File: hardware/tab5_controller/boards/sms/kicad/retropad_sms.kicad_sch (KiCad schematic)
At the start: 46 parts, among them J1 Tab5 Ext.Port1, J2 SWD, SW1 UP, SW10 START, SW11 MENU, SW12 L, SW13 R, SW2 DOWN, SW3 LEFT, SW4 RIGHT, SW5 X, SW6 B, SW7 Y, SW8 A, SW9 SELECT, U1 STM32F030C8T6

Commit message: tab5_controller: NES, Game Boy, Genesis and SMS/GG boards; shared generators
Generators move from boards/snes/kicad to boards/kicad_gen and take a
console name (gen_pcb.py, gen_sch.py, check_netlist.py, plus render.py);
console ids, titles and ID straps come from layout.CONSOLES.

New layouts in layout.py, each passing the clearance checks:
- NES (ID 1): B/A side by side, flat SELECT/START, MENU
- Game Boy (ID 2): diagonal B/A, flat SELECT/START (the angled pair left
  ROW7 unroutable), MENU
- Genesis (ID 5): A/B/C rising row, START, MENU
- Master System / Game Gear (ID 4): 1/2 on the B/A bits, START, MENU

All five boards are regenerated: routed with 0 unconnected pads and no
clearance/edge errors, schematic vs PCB 0 differences, ID straps and
button matrix wiring verified. Connector GND pins and SMD pads now join
the GND pour solidly, which removes starved-thermal errors.

Co-Authored-By: Claude Opus 5.5 <noreply@anthropic.com>
Claude-Session: https://claude.ai/code/session_01NhSHTsezreiVZCnuBhQzP2
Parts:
- removed D10, D11, D12, D13, D9: 1N4148W, Diode_SMD:D_SOD-123, symbol Device:D
- removed SW10: START, Button_Switch_THT:SW_PUSH_6mm, symbol Switch:SW_Push
- removed SW11: MENU, Button_Switch_THT:SW_PUSH_6mm, symbol Switch:SW_Push
- removed SW12: L, Button_Switch_THT:SW_Tactile_SPST_Angled_PTS645Vx31-2LFS, symbol Switch:SW_Push
- removed SW13: R, Button_Switch_THT:SW_Tactile_SPST_Angled_PTS645Vx31-2LFS, symbol Switch:SW_Push
- removed SW9: SELECT, Button_Switch_THT:SW_PUSH_6mm, symbol Switch:SW_Push
- R6, R7: value 0R -> DNP; now not fitted; now left out of the parts list
- R8: value DNP -> 0R; now fitted; now in the parts list
- SW5: value X -> 1
- SW6: value B -> 2
- SW7: value Y -> START; footprint Button_Switch_THT:SW_PUSH-12mm -> Button_Switch_THT:SW_PUSH_6mm
- SW8: value A -> MENU; footprint Button_Switch_THT:SW_PUSH-12mm -> Button_Switch_THT:SW_PUSH_6mm
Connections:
- net K_A is gone; now on net K_MENU: D8.1 (K), SW8.1
- net K_Y is gone; now on net K_START: D7.1 (K), SW7.1
- net COL0: no longer SW8.2
- net COL2: now also SW8.2
- net ROW0: now also D8.2 (A); no longer D7.2 (A)
- net ROW4: now also D6.2 (A); no longer D8.2 (A)
- net ROW5: now also D5.2 (A); no longer D6.2 (A)
- net ROW6: now also D7.2 (A)
- net ROW7: no longer D5.2 (A)
- net K_B renamed K_2
- net K_X renamed K_1
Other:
- note added: "1"
- note added: "2"
- note added: "Console ID straps: 0R to GND = bit set. Master System / Game Gear = ID 4 (fit R8; R6, R7, R9, R10 DNP)"
- note removed: "A"
- note removed: "B"
- note removed: "Console ID straps: 0R to GND = bit set. SNES = ID 3 (fit R6, R7; R8, R9, R10 DNP)"
- note removed: "L"
- note removed: "R"
- note removed: "SELECT"
- note removed: "X"
- note removed: "Y"
- title: RetroPad SNES controller (console ID 3) -> RetroPad Master System / Game Gear controller (console ID 4)

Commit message: tab5_controller: build every console board on the AVR32DD28
The STM32F030 matrix boards are gone. SNES, NES, Game Boy, Genesis and
Master System / Game Gear are now all AVR32DD28 boards: one MCU pin per
button, no diodes, UPDI programming, one firmware image (firmware_avrdd)
keyed by the console-ID straps.

- layout.py / gen_pcb.py / gen_sch.py: drop the stm32 core (LQFP-48,
  key matrix, diodes, SWD header, AN_EN strap); the AVR DD core is the
  only one, and the *_dd board names become the plain console names.
- SNES, NES and Genesis keep the routing of their AVR DD prototypes;
  Game Boy and Master System are routed fresh.
- Every board: DRC 0 unconnected (silkscreen warnings only), schematic
  vs PCB 0 differences, and each switch checked against the MCU pin
  pinmap.h gives it for that console ID.
- Host test now also covers the Game Boy and Master System pin maps.
- READMEs describe the AVR DD boards only.

Co-Authored-By: Claude Opus 5.5 <noreply@anthropic.com>
Claude-Session: https://claude.ai/code/session_01NhSHTsezreiVZCnuBhQzP2
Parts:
- removed C5: 100nF, Capacitor_SMD:C_0603_1608Metric, symbol Device:C
- removed D1, D2, D3, D4, D5, D6, D7, D8: 1N4148W, Diode_SMD:D_SOD-123, symbol Device:D
- removed R10: DNP, Resistor_SMD:R_0603_1608Metric, symbol Device:R
- removed R4, R5: 10k, Resistor_SMD:R_0603_1608Metric, symbol Device:R
- added R11: DNP, Resistor_SMD:R_0603_1608Metric, symbol Device:R
- J2: value SWD -> UPDI; footprint Connector_PinHeader_2.54mm:PinHeader_1x05_P2.54mm_Vertical -> Connector_PinHeader_2.54mm:PinHeader_1x03_P2.54mm_Vertical; symbol Connector_Generic:Conn_01x05 -> Connector_Generic:Conn_01x03
- U1: value STM32F030C8T6 -> AVR32DD28-I/SO; footprint Package_QFP:LQFP-48_7x7mm_P0.5mm -> Package_SO:SOIC-28W_7.5x17.9mm_P1.27mm; symbol MCU_ST_STM32F0:STM32F030C8Tx -> RetroPad:AVR32DD28-xSO
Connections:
- net COL3 is gone; now on net K_START: U1.13 (PD7)
- net ROW2 is gone; now on net +3V3: U1.20 (VDD)
- net +3V3: now also U1.14 (VDD), U1.6 (VDDIO2); no longer U1.1 (VDD), U1.24 (VDD), U1.48 (VDD), U1.9 (VDDA)
- net GND: now also J2.3 (Pin_3), SW1.2, SW2.2, SW3.2, SW4.2, SW5.2, SW6.2, SW7.2, SW8.2, U1.15 (GND), U1.21 (GND); no longer J2.5 (Pin_5), U1.23 (VSS), U1.47 (VSS), U1.8 (VSSA)
- net ID0: now also U1.22 (XTALHF1/PA0); no longer U1.25 (PB12)
- net ID1: now also U1.23 (XTALHF2/PA1); no longer U1.26 (PB13)
- net ID2: now also U1.28 (PA6); no longer U1.27 (PB14)
- net ID3: now also U1.1 (PA7); no longer U1.45 (PB8)
- net K_1: now also U1.11 (PD5)
- net K_2: now also U1.12 (PD6)
- net K_DOWN: now also U1.8 (PD2)
- net K_LEFT: now also U1.9 (PD3)
- net K_MENU: now also U1.2 (PC0)
- net K_RIGHT: now also U1.10 (PD4)
- net K_UP: now also U1.7 (PD1)
- net SCL: now also U1.25 (PA3); no longer U1.21 (PB10)
- net SDA: now also U1.24 (PA2); no longer U1.22 (PB11)
- net G9_UPDI: now reaches J1.10 (Pin_10)
- net G9_UPDI: now also R11.2
- removed net AN_EN: U1.46 (PB9)
- removed net BOOT0: U1.44 (BOOT0)
- removed net COL0: SW1.2, SW2.2, SW3.2, SW4.2, SW5.2, SW6.2, U1.10 (PA0)
- removed net COL1: SW7.2, U1.11 (PA1)
- removed net COL2: SW8.2, U1.12 (PA2)
- removed net INT: J1.9 (Pin_9), R3.2, U1.38 (PA15)
- removed net NRST: J2.4 (Pin_4), U1.7 (NRST)
- net ROW0 renamed RESET
- net RESET: now also R3.2
- net ROW1 renamed UPDI
- net UPDI: now also J2.2 (Pin_2), R11.1
- removed net ROW3: U1.39 (PB3)
- removed net ROW4: U1.40 (PB4)
- removed net ROW5: U1.41 (PB5)
- removed net ROW6: U1.42 (PB6)
- removed net ROW7: U1.43 (PB7)
- removed net SWCLK: J2.2 (Pin_2), U1.37 (PA14)
- removed net SWDIO: J2.3 (Pin_3), U1.34 (PA13)
- new net AN0: U1.26 (PA4)
- new net AN1: U1.27 (PA5)
- no-connect marks 20 -> 8
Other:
- note added: "Buttons — one MCU pin each, switch to GND (internal pull-up); slot table in firmware_avrdd/pinmap.h"
- note added: "Console ID straps: 0R to GND = bit set. Master System / Game Gear = ID 4 (fit R8; R6, R7, R9 DNP)"
- note added: "Decoupling (VDD x2, VDDIO2), I2C pull-ups, RESET pull-up"
- note added: "MCU — AVR32DD28 (SOIC-28) running firmware_avrdd (I2C client 0x6D, RetroPad protocol)"
- note added: "PD1-PD7, PC0-PC3, PF0-PF1: one button per pin (internal pull-ups)"
- note added: "R11 (DNP): UPDI to J1 pin 10 / G9 — experimental in-system programming from the Tab5"
- note added: "UPDI programming (SerialUPDI / MPLAB Snap)"
- note removed: "Button matrix — row driven high, column read with pull-down; diode anode on the row"
- note removed: "Console ID straps: 0R to GND = bit set. Master System / Game Gear = ID 4 (fit R8; R6, R7, R9, R10 DNP)"
- note removed: "Decoupling, pull-ups, reset, BOOT0 (copied from the M5Stack keyboard)"
- note removed: "MCU — STM32F030C8T6 running the RetroPad firmware (I2C slave 0x6D)"
- note removed: "SWD (same order as the keyboard's P2)"
- moved on the sheet: C4, SW1, SW2, SW3, SW4, SW5, SW6, SW7, SW8

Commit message: tab5_controller: remove the UPDI-to-G9 link (R11) from every board
The Tab5 never updates controller firmware, so J1 pin 10 (G9) is left
unconnected, as on M5Stack's keyboard, and R11 and the G9_UPDI net are
gone. Boards are programmed only through their own UPDI header J2.

All five boards are re-routed (the old routes ended at R11). Game Boy
is routed with Freerouting 2.1 single-threaded because 1.9 stalls with
UPDI unrouted on it. Every board: DRC 0 unconnected pads (silkscreen
warnings only), schematic vs PCB 0 differences, switches on the pins
pinmap.h expects.

Co-Authored-By: Claude Opus 5.5 <noreply@anthropic.com>
Claude-Session: https://claude.ai/code/session_01NhSHTsezreiVZCnuBhQzP2
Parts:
- removed R11: DNP, Resistor_SMD:R_0603_1608Metric, symbol Device:R
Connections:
- net G9_UPDI: no longer names the net of J1.10 (Pin_10)
- no-connect marks 8 -> 9
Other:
- note removed: "R11 (DNP): UPDI to J1 pin 10 / G9 — experimental in-system programming from the Tab5"
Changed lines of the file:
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@@
       (project "retropad_sms" (path "/a309cff3-1dfb-5baa-b184-d84380f3c827" (reference "J1") (unit 1)))))
   (no_connect (at 170.18 39.37))
-  (wire
-    (pts (xy 182.88 49.53) (xy 190.5 49.53))
-    (stroke (width 0) (type default))
-)
-  (global_label
-    "G9_UPDI"
-    (shape bidirectional)
-    (at 190.5 49.53 0)
-    (fields_autoplaced)
-    (effects (font (size 1.27 1.27)) (justify left))
-    (property
-      "Intersheetrefs"
-      "${INTERSHEET_REFS}"
-      (at 190.5 49.53 0)
-      (effects (font (size 1.27 1.27)) hide)))
+  (no_connect (at 182.88 49.53))
   (wire
     (pts (xy 182.88 39.37) (xy 190.5 39.37))
@@
         (path "/a309cff3-1dfb-5baa-b184-d84380f3c827" (reference "#PWR17") (unit 1)))))
   (text
-    "R11 (DNP): UPDI to J1 pin 10 / G9 — experimental in-system programming from the Tab5"
-    (at 150 200 0)
-    (effects (font (size 1.27 1.27)) (justify left))
-)
-  (symbol
-    (lib_id "Device:R")
-    (at 234.95 190.5 0)
-    (unit 1)
-    (in_bom no)
-    (on_board yes)
-    (dnp yes)
-    (property "Reference" "R11" (at 237.49 189.23 0) (effects (font (size 1.27 1.27)) (justify left)))
-    (property "Value" "DNP" (at 237.49 191.77 0) (effects (font (size 1.27 1.27)) (justify left)))
-    (property
-      "Footprint"
-      "Resistor_SMD:R_0603_1608Metric"
-      (at 234.95 190.5 0)
-      (effects (font (size 1.27 1.27)) hide))
-    (property "Datasheet" "~" (at 234.95 190.5 0) (effects (font (size 1.27 1.27)) hide))
-    (pin "1")
-    (pin "2")
-    (instances
-      (project "retropad_sms" (path "/a309cff3-1dfb-5baa-b184-d84380f3c827" (reference "R11") (unit 1)))))
-  (wire
-    (pts (xy 234.95 186.69) (xy 234.95 184.15))
-    (stroke (width 0) (type default))
-)
-  (global_label
-    "UPDI"
-    (shape bidirectional)
-    (at 234.95 184.15 90)
-    (fields_autoplaced)
-    (effects (font (size 1.27 1.27)) (justify left))
-    (property
-      "Intersheetrefs"
-      "${INTERSHEET_REFS}"
-      (at 234.95 184.15 0)
-      (effects (font (size 1.27 1.27)) hide)))
-  (wire
-    (pts (xy 234.95 194.31) (xy 234.95 196.85))
-    (stroke (width 0) (type default))
-)
-  (global_label
-    "G9_UPDI"
-    (shape bidirectional)
-    (at 234.95 196.85 270)
-    (fields_autoplaced)
-    (effects (font (size 1.27 1.27)) (justify right))
-    (property
-      "Intersheetrefs"
-      "${INTERSHEET_REFS}"
-      (at 234.95 196.85 0)
-      (effects (font (size 1.27 1.27)) hide)))
-  (text
     "Mounting holes (M3, 96 mm apart)"

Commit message: tab5_controller: 0805 hand-solder passives on every board
Swap the 0603 resistors and capacitors (decoupling, I2C pull-ups, reset
pull-up, console-ID straps) for KiCad's 0805 HandSolder footprints, which
have longer pads for soldering by hand. C2 turns 90 degrees so its larger
courtyard clears U1. All four boards are re-routed with Freerouting 1.9;
schematics, BOMs, DRC reports and renders are regenerated.

DRC: 0 errors and 0 unconnected pads on every board (silkscreen and
library-path warnings only). Schematic vs PCB: 0 differences.

Co-Authored-By: Claude Opus 5.5 <noreply@anthropic.com>
Claude-Session: https://claude.ai/code/session_016pgTnJvu7Wh4anaUwDfFmN
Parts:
- C1, C2, C3, C4: footprint Capacitor_SMD:C_0603_1608Metric -> Capacitor_SMD:C_0805_2012Metric_Pad1.18x1.45mm_HandSolder
- R1, R2, R3, R6, R7, R8, R9: footprint Resistor_SMD:R_0603_1608Metric -> Resistor_SMD:R_0805_2012Metric_Pad1.20x1.40mm_HandSolder
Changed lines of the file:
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@@
     (property
       "Footprint"
-      "Capacitor_SMD:C_0603_1608Metric"
+      "Capacitor_SMD:C_0805_2012Metric_Pad1.18x1.45mm_HandSolder"
       (at 160.02 129.54 0)
       (effects (font (size 1.27 1.27)) hide))
@@
     (property
       "Footprint"
-      "Capacitor_SMD:C_0603_1608Metric"
+      "Capacitor_SMD:C_0805_2012Metric_Pad1.18x1.45mm_HandSolder"
       (at 175.26 129.54 0)
       (effects (font (size 1.27 1.27)) hide))
@@
     (property
       "Footprint"
-      "Capacitor_SMD:C_0603_1608Metric"
+      "Capacitor_SMD:C_0805_2012Metric_Pad1.18x1.45mm_HandSolder"
       (at 190.5 129.54 0)
       (effects (font (size 1.27 1.27)) hide))
@@
     (property
       "Footprint"
-      "Capacitor_SMD:C_0603_1608Metric"
+      "Capacitor_SMD:C_0805_2012Metric_Pad1.18x1.45mm_HandSolder"
       (at 204.47 129.54 0)
       (effects (font (size 1.27 1.27)) hide))
@@
     (property
       "Footprint"
-      "Resistor_SMD:R_0603_1608Metric"
+      "Resistor_SMD:R_0805_2012Metric_Pad1.20x1.40mm_HandSolder"
       (at 160.02 154.94 0)
       (effects (font (size 1.27 1.27)) hide))
@@
     (property
       "Footprint"
-      "Resistor_SMD:R_0603_1608Metric"
+      "Resistor_SMD:R_0805_2012Metric_Pad1.20x1.40mm_HandSolder"
       (at 175.26 154.94 0)
       (effects (font (size 1.27 1.27)) hide))
@@
     (property
       "Footprint"
-      "Resistor_SMD:R_0603_1608Metric"
+      "Resistor_SMD:R_0805_2012Metric_Pad1.20x1.40mm_HandSolder"
       (at 190.5 154.94 0)
       (effects (font (size 1.27 1.27)) hide))
@@
     (property
       "Footprint"
-      "Resistor_SMD:R_0603_1608Metric"
+      "Resistor_SMD:R_0805_2012Metric_Pad1.20x1.40mm_HandSolder"
       (at 160.02 190.5 0)
       (effects (font (size 1.27 1.27)) hide))
@@
     (property
       "Footprint"
-      "Resistor_SMD:R_0603_1608Metric"
+      "Resistor_SMD:R_0805_2012Metric_Pad1.20x1.40mm_HandSolder"
       (at 175.26 190.5 0)
       (effects (font (size 1.27 1.27)) hide))
@@
     (property
       "Footprint"
-      "Resistor_SMD:R_0603_1608Metric"
+      "Resistor_SMD:R_0805_2012Metric_Pad1.20x1.40mm_HandSolder"
       (at 190.5 190.5 0)
       (effects (font (size 1.27 1.27)) hide))
@@
     (property
       "Footprint"
-      "Resistor_SMD:R_0603_1608Metric"
+      "Resistor_SMD:R_0805_2012Metric_Pad1.20x1.40mm_HandSolder"
       (at 204.47 190.5 0)
       (effects (font (size 1.27 1.27)) hide))

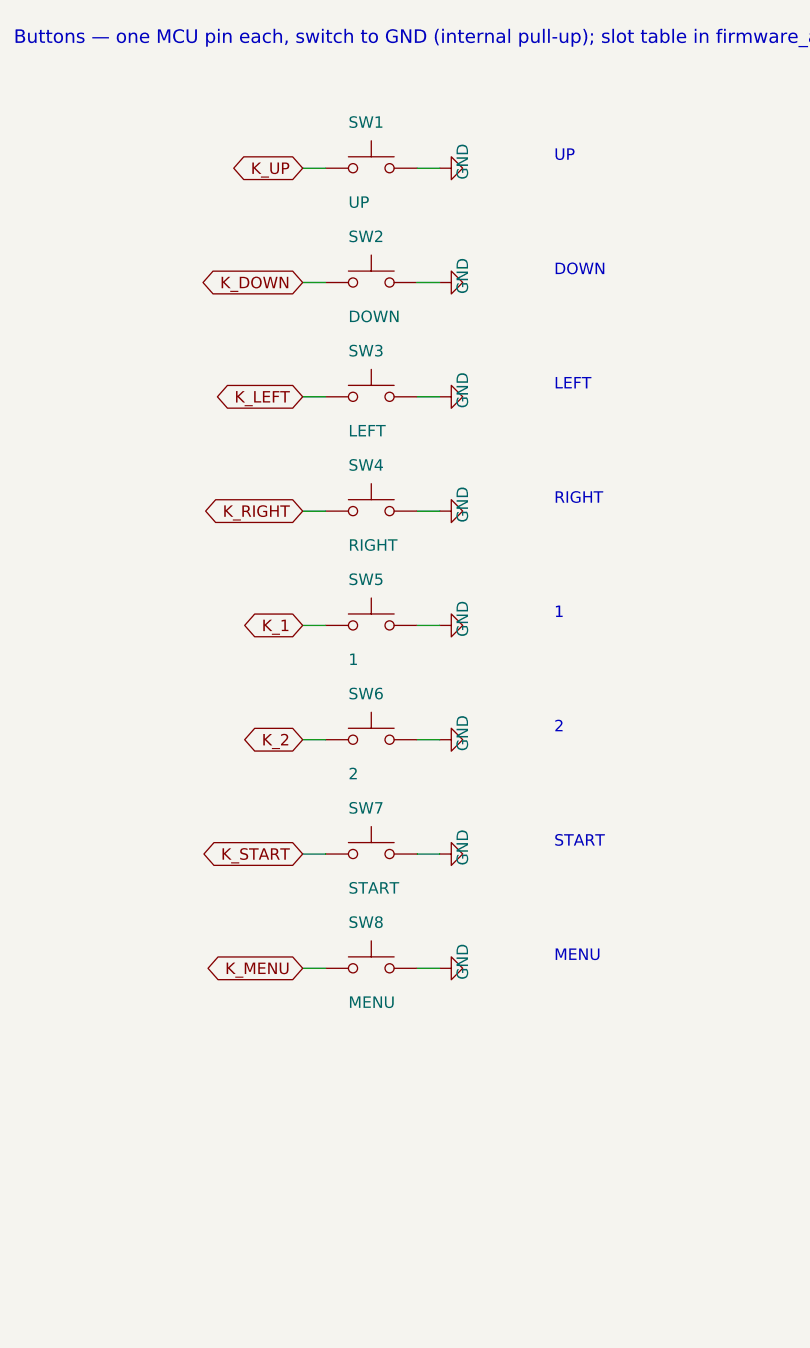
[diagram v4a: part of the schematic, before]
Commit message: tab5_controller: 4-pin tact switch symbols and footprints
The 6x6 and 12x12 switches are 4-leg parts, and the production layout in
EasyEDA uses their 4-pin symbols, so the KiCad boards now match:

- kicad_lib/RetroPad.pretty: SW_PUSH_6mm_4pin and SW_PUSH-12mm_4pin,
  KiCad's footprints with the pads renumbered 1-4 (pad 1 top-left, then
  clockwise; tied pairs 1-2 and 3-4, the legs 6.5 / 12.5 mm apart).
  gen_pcb.py writes them from the stock footprints and points each
  board's fp-lib-table at the library.
- RetroPad:SW_Push_4pin symbol in gen_sch.py: 1-2 tied, 4-3 tied, one
  contact between. KiCad's 4-pin SW_Push_Dual is a two-contact switch,
  so it doesn't fit these parts.
- Wiring: legs 1-2 to GND, 3-4 to K_<button>. L/R (right angle, two
  contacts plus mounting legs) keep the 2-pin SW_Push.
- All four boards re-routed: DRC 0 unconnected (silkscreen warnings
  only), schematic vs PCB 0 differences, every switch on the pin
  pinmap.h expects; firmware host test passes; Gerber/drill export OK.

Co-Authored-By: Claude Opus 5.5 <noreply@anthropic.com>
Claude-Session: https://claude.ai/code/session_01NhSHTsezreiVZCnuBhQzP2
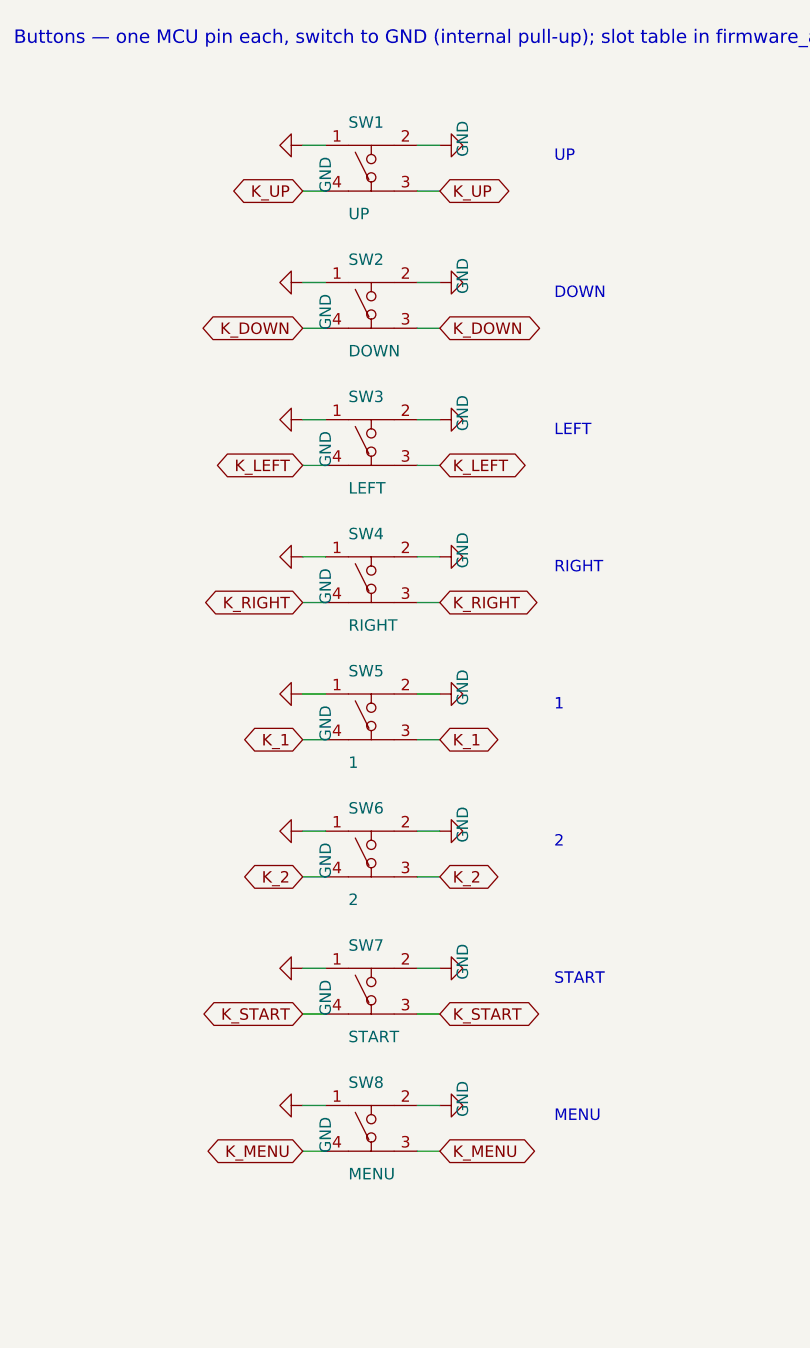
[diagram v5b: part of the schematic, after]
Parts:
- SW1, SW2, SW3, SW4, SW7, SW8: footprint Button_Switch_THT:SW_PUSH_6mm -> RetroPad:SW_PUSH_6mm_4pin; symbol Switch:SW_Push -> RetroPad:SW_Push_4pin
- SW5, SW6: footprint Button_Switch_THT:SW_PUSH-12mm -> RetroPad:SW_PUSH-12mm_4pin; symbol Switch:SW_Push -> RetroPad:SW_Push_4pin
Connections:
- net GND: now also SW1.1, SW2.1, SW3.1, SW4.1, SW5.1, SW6.1, SW7.1, SW8.1
- net K_1: now also SW5.3, SW5.4; no longer SW5.1
- net K_2: now also SW6.3, SW6.4; no longer SW6.1
- net K_DOWN: now also SW2.3, SW2.4; no longer SW2.1
- net K_LEFT: now also SW3.3, SW3.4; no longer SW3.1
- net K_MENU: now also SW8.3, SW8.4; no longer SW8.1
- net K_RIGHT: now also SW4.3, SW4.4; no longer SW4.1
- net K_START: now also SW7.3, SW7.4; no longer SW7.1
- net K_UP: now also SW1.3, SW1.4; no longer SW1.1
